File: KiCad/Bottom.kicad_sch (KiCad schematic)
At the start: 31 parts, among them J162 Screw_Terminal_01x02

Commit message: WIP on Bottom
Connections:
- net +3.3V: now also U?.16 (GPIO12)
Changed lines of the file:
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@@
+    (effects (font (size 1.27 1.27)) (justify right))
+  )
+  (hierarchical_label "+3.3V" (shape input) (at 96.52 113.03 180) (fields_autoplaced)
     (effects (font (size 1.27 1.27)) (justify right))
   )

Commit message: Layout wip
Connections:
- net SPI1_CSn renamed SPI_CSn_BOT
- net SPI1_RST renamed SPI0_RST
- net SPI1_RX renamed SPI_RX_BOT
- net SPI1_SCK renamed SPI_SCK_BOT
- net SPI1_TX renamed SPI_TX_BOT
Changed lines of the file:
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@@
     (effects (font (size 1.27 1.27)) (justify left bottom))
   )
-  (label "SPI1_RST" (at 85.09 100.33 0) (fields_autoplaced)
+  (label "SPI0_RST" (at 85.09 100.33 0) (fields_autoplaced)
     (effects (font (size 1.27 1.27)) (justify left bottom))
   )
@@
     (effects (font (size 1.27 1.27)) (justify left bottom))
   )
-  (label "SPI1_RST" (at 113.03 35.56 0) (fields_autoplaced)
+  (label "SPI0_RST" (at 113.03 35.56 0) (fields_autoplaced)
     (effects (font (size 1.27 1.27)) (justify left bottom))
   )
@@
     (effects (font (size 1.27 1.27)) (justify left bottom))
   )
-  (label "SPI0_RX" (at 35.56 129.54 0) (fields_autoplaced)
+  (label "SPI1_RX" (at 35.56 129.54 0) (fields_autoplaced)
     (effects (font (size 1.27 1.27)) (justify left bottom))
   )
@@
     (effects (font (size 1.27 1.27)) (justify left bottom))
   )
-  (label "SPI1_CSn" (at 113.03 27.94 0) (fields_autoplaced)
+  (label "SPI0_CSn" (at 113.03 27.94 0) (fields_autoplaced)
     (effects (font (size 1.27 1.27)) (justify left bottom))
   )
@@
     (effects (font (size 1.27 1.27)) (justify left bottom))
   )
-  (label "SPI0_CSn" (at 35.56 132.08 0) (fields_autoplaced)
+  (label "SPI1_CSn" (at 35.56 132.08 0) (fields_autoplaced)
     (effects (font (size 1.27 1.27)) (justify left bottom))
   )
@@
     (effects (font (size 1.27 1.27)) (justify left bottom))
   )
-  (label "SPI0_TX" (at 35.56 137.16 0) (fields_autoplaced)
+  (label "SPI1_TX" (at 35.56 137.16 0) (fields_autoplaced)
     (effects (font (size 1.27 1.27)) (justify left bottom))
   )
@@
     (effects (font (size 1.27 1.27)) (justify left bottom))
   )
-  (label "SPI1_TX" (at 113.03 33.02 0) (fields_autoplaced)
+  (label "SPI0_TX" (at 113.03 33.02 0) (fields_autoplaced)
     (effects (font (size 1.27 1.27)) (justify left bottom))
   )
-  (label "SPI0_SCK" (at 35.56 134.62 0) (fields_autoplaced)
+  (label "SPI1_SCK" (at 35.56 134.62 0) (fields_autoplaced)
     (effects (font (size 1.27 1.27)) (justify left bottom))
   )
@@
     (effects (font (size 1.27 1.27)) (justify left bottom))
   )
-  (label "SPI1_SCK" (at 113.03 30.48 0) (fields_autoplaced)
+  (label "SPI0_SCK" (at 113.03 30.48 0) (fields_autoplaced)
     (effects (font (size 1.27 1.27)) (justify left bottom))
   )
@@
     (effects (font (size 1.27 1.27)) (justify left bottom))
   )
-  (hierarchical_label "SPI0_TX" (shape input) (at 29.21 137.16 180) (fields_autoplaced)
+  (hierarchical_label "SPI_TX_BOT" (shape input) (at 29.21 137.16 180) (fields_autoplaced)
     (effects (font (size 1.27 1.27)) (justify right))
   )
@@
     (effects (font (size 1.27 1.27)) (justify right))
   )
-  (hierarchical_label "SPI0_CSn" (shape input) (at 29.21 132.08 180) (fields_autoplaced)
+  (hierarchical_label "SPI_CSn_BOT" (shape input) (at 29.21 132.08 180) (fields_autoplaced)
     (effects (font (size 1.27 1.27)) (justify right))
   )
-  (hierarchical_label "SPI0_SCK" (shape input) (at 29.21 134.62 180) (fields_autoplaced)
+  (hierarchical_label "SPI_SCK_BOT" (shape input) (at 29.21 134.62 180) (fields_autoplaced)
     (effects (font (size 1.27 1.27)) (justify right))
   )
@@
     (effects (font (size 1.27 1.27)) (justify right))
   )
-  (hierarchical_label "SPI0_RX" (shape input) (at 29.21 129.54 180) (fields_autoplaced)
+  (hierarchical_label "SPI_RX_BOT" (shape input) (at 29.21 129.54 180) (fields_autoplaced)
     (effects (font (size 1.27 1.27)) (justify right))
   )

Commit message: Ready for review
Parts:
- U?: footprint Module_RaspberryPi_Pico:RaspberryPi_Pico_Original_SMD_Castellated_HandSolder -> Module_RaspberryPi_Pico:RaspberryPi_Pico_Common_No_Keepout
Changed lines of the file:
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@@
       (effects (font (size 1.27 1.27)) (justify left))
     )
-    (property "Footprint" "Module_RaspberryPi_Pico:RaspberryPi_Pico_Original_SMD_Castellated_HandSolder" (at 119.38 154.94 0)
+    (property "Footprint" "Module_RaspberryPi_Pico:RaspberryPi_Pico_Common_No_Keepout" (at 119.38 154.94 0)
       (effects (font (size 1.27 1.27)) hide)
     )

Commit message: Updated to generate JLCPCB files
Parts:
- added C127: RVT0J102M0810, footprint:CAP-SMD_BD8.0-L8.3-W8.3-FD, symbol RVT0J102M0810:RVT0J102M0810
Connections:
- net GND: now also C127.2
- net VDD: now also C127.1
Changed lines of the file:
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@@
+    (effects (font (size 1.27 1.27)) (justify right))
+  )
+  (hierarchical_label "GND" (shape input) (at 242.57 48.26 270) (fields_autoplaced)
     (effects (font (size 1.27 1.27)) (justify right))
   )
@@
   (hierarchical_label "GND" (shape input) (at 231.14 67.31 180) (fields_autoplaced)
     (effects (font (size 1.27 1.27)) (justify right))
+  )
+  (hierarchical_label "VDD" (shape input) (at 242.57 40.64 90) (fields_autoplaced)
+    (effects (font (size 1.27 1.27)) (justify left))
   )
   (hierarchical_label "VDD" (shape input) (at 119.38 48.26 90) (fields_autoplaced)
@@
         )
       )
+    )
+  )
+  (symbol (lib_id "RVT0J102M0810:RVT0J102M0810") (at 242.57 44.45 0) (unit 1)
+    (in_bom yes) (on_board yes) (dnp no) (fields_autoplaced)
+    (property "Reference" "C127" (at 246.38 41.9139 0)
+      (effects (font (size 1.27 1.27)) (justify left))
+    )
+    (property "Value" "RVT0J102M0810" (at 246.38 44.4539 0)
+      (effects (font (size 1.27 1.27)) (justify left))
+    )
+    (property "Footprint" "footprint:CAP-SMD_BD8.0-L8.3-W8.3-FD" (at 242.57 54.61 0)
+      (effects (font (size 1.27 1.27) italic) hide)
+    )
+    (property "Datasheet" "https://item.szlcsc.com/245644.html" (at 240.284 44.323 0)
+      (effects (font (size 1.27 1.27)) (justify left) hide)
+    )
+    (property "LCSC" "C42851" (at 242.57 44.45 0)
+      (effects (font (size 1.27 1.27)) hide)
+    )
+    (pin "1")
+    (pin "2")
+    (instances
+      (project "Kaboom_box"
+        (path "/8d340784-229e-46d1-990c-7f8852f9fc49/d111de2c-3c3c-486e-8c4b-bd3963817676"
+          (reference "C127") (unit 1)
+        )
+      )

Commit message: PCB V1
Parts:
- R? (x2): now not fitted
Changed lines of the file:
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@@
   )
   (symbol (lib_id "0805W8F0000T5E:0805W8F0000T5E") (at 267.97 66.04 0) (unit 1)
-    (in_bom yes) (on_board yes) (dnp no) (fields_autoplaced)
+    (in_bom yes) (on_board yes) (dnp yes) (fields_autoplaced)
     (property "Reference" "R?" (at 267.97 59.69 0)
       (effects (font (size 1.27 1.27)))
@@
   )
   (symbol (lib_id "0805W8F0000T5E:0805W8F0000T5E") (at 267.97 76.2 0) (unit 1)
-    (in_bom yes) (on_board yes) (dnp no) (fields_autoplaced)
+    (in_bom yes) (on_board yes) (dnp yes) (fields_autoplaced)
     (property "Reference" "R?" (at 267.97 69.85 0)
       (effects (font (size 1.27 1.27)))

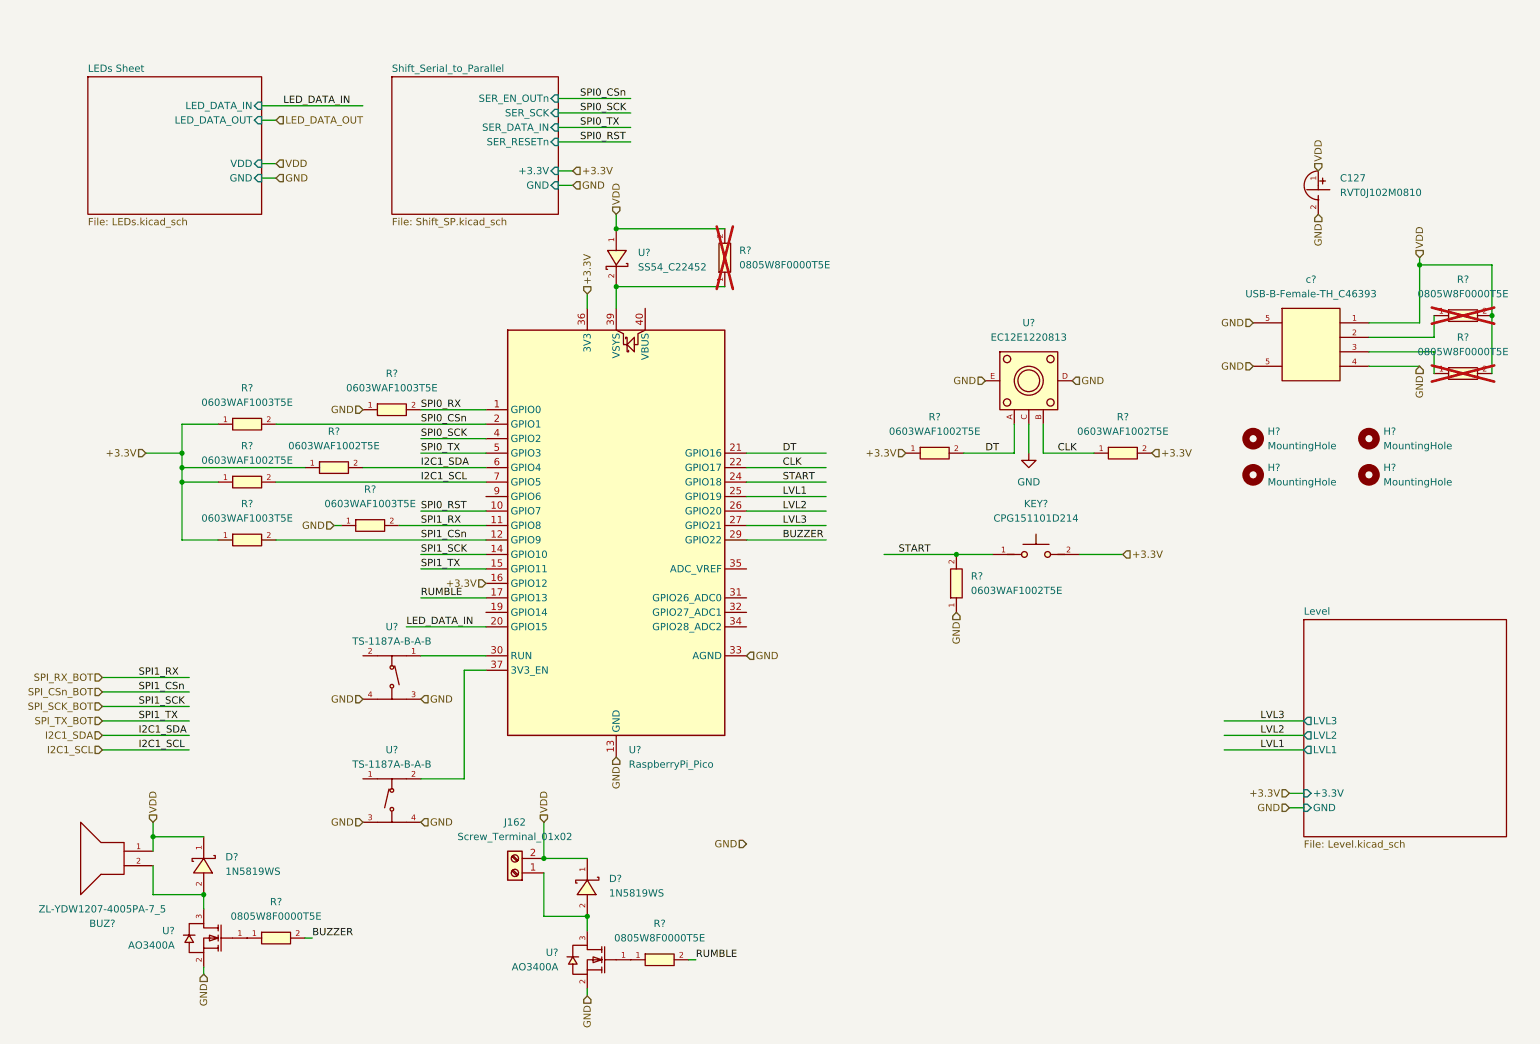
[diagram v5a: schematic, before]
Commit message: UPdated outline + added pull down resistors on input of shifts
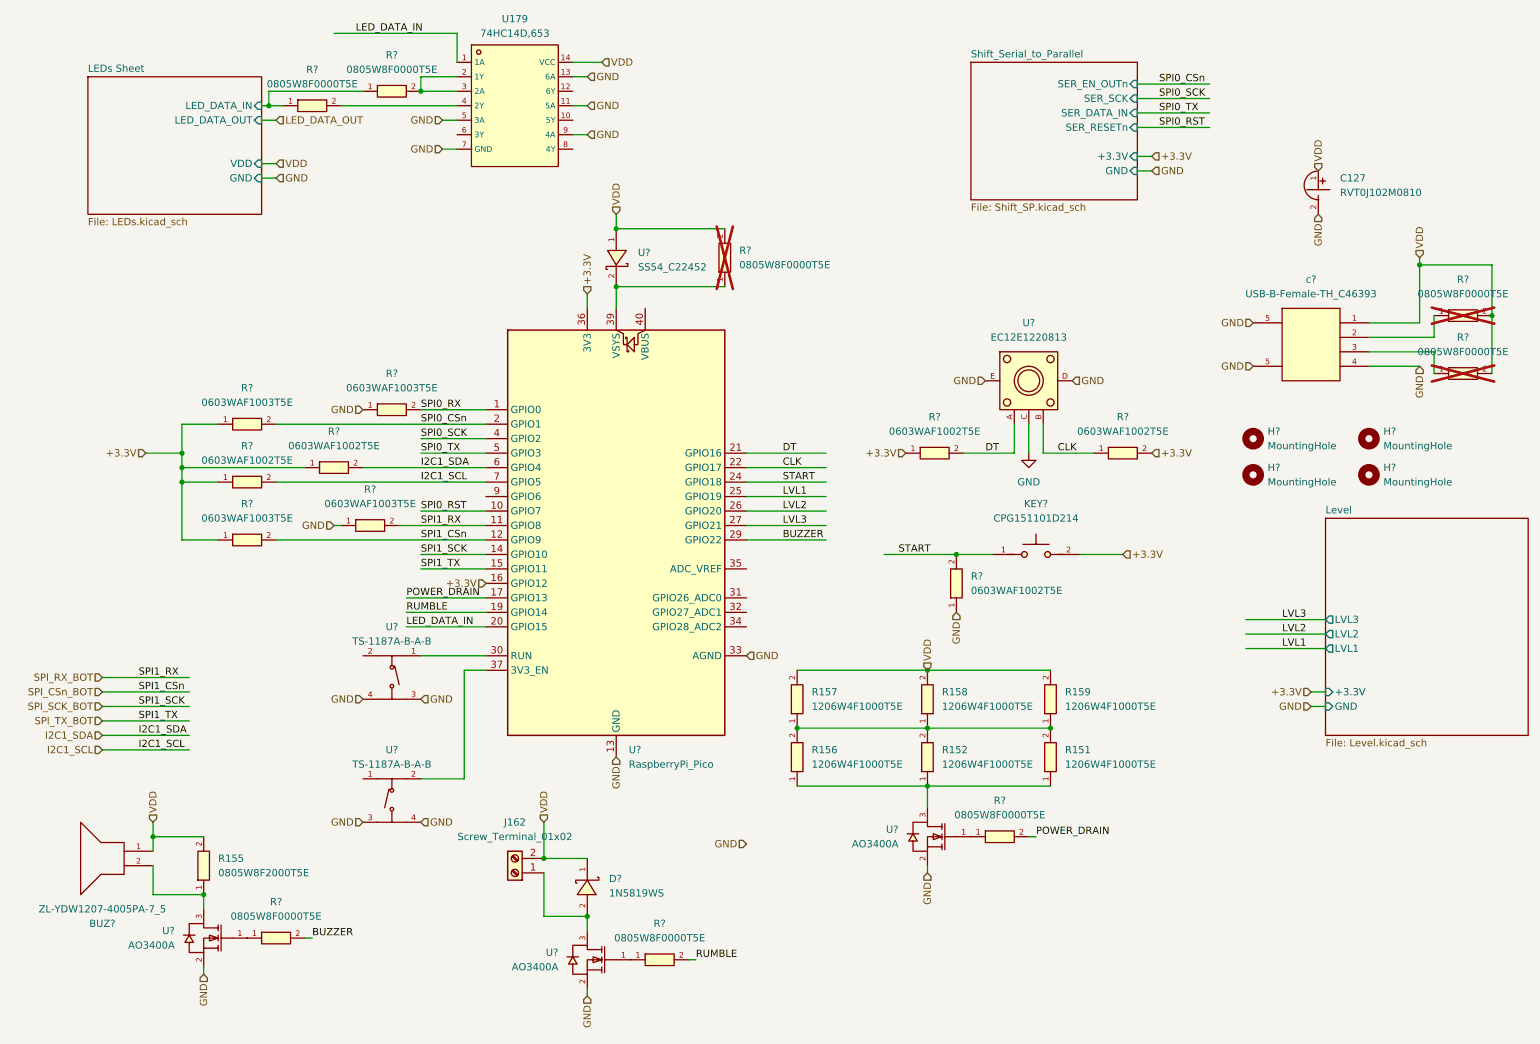
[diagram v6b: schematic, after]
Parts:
- removed D?: 1N5819WS, footprint:SOD-323_L1.8-W1.3-LS2.5-RD, symbol 1N5819WS:1N5819WS
- added R151, R152, R156, R157, R158, R159: 1206W4F1000T5E, footprint:R1206, symbol 1206W4F1000T5E:1206W4F1000T5E
- added R155: 0805W8F2000T5E, footprint:R0805, symbol 0805W8F2000T5E:0805W8F2000T5E
- added R? (x3): 0805W8F0000T5E, footprint:R0805, symbol 0805W8F0000T5E:0805W8F0000T5E
- added U179: 74HC14D,653, footprint:SOIC-14_L8.7-W3.9-P1.27-LS6.0-BL, symbol 74HC14D,653:74HC14D,653
- added U?: AO3400A, footprint:SOT-23-3_L2.9-W1.6-P1.90-LS2.8-BR, symbol AO3400A:AO3400A
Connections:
- net GND: now also U179.11 (5A), U179.13 (6A), U179.5 (3A), U179.7 (GND), U179.9 (4A), U?.2 (S)
- net LED_DATA_IN: now also U179.1 (1A)
- net RUMBLE: now also U?.19 (GPIO14); no longer U?.17 (GPIO13)
- net VDD: now also R155.2, R157.2, R158.2, R159.2, U179.14 (VCC)
- net at BUZ?.2, U?.3 (D): now also R155.1
- new net: R?.2, U179.2 (1Y), U179.3 (2A)
- new net: R?.2, U179.4 (2Y)
- new net: R151.2, R152.2, R156.2, R157.1, R158.1, R159.1
- new net: R151.1, R152.1, R156.1, U?.3 (D)
- new net: R?.1, U?.1 (G)
- new net LEDs Sheet/LED_DATA_IN: R?.1, R?.1
- new net POWER_DRAIN: R?.2, U?.17 (GPIO13)

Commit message: Updates for V2
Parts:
- added C?: CC0603KRX7R9BB104, footprint:C0603, symbol CC0603KRX7R9BB104:CC0603KRX7R9BB104
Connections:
- net GND: now also C?.2
- net VDD: now also C?.1
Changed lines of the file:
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@@
+    (effects (font (size 1.27 1.27)) (justify right))
+  )
+  (hierarchical_label "VDD" (shape input) (at 96.52 48.26 180) (fields_autoplaced)
     (effects (font (size 1.27 1.27)) (justify right))
   )
@@
   )
   (hierarchical_label "VDD" (shape input) (at 242.57 40.64 90) (fields_autoplaced)
+    (effects (font (size 1.27 1.27)) (justify left))
+  )
+  (hierarchical_label "GND" (shape input) (at 106.68 48.26 0) (fields_autoplaced)
     (effects (font (size 1.27 1.27)) (justify left))
   )
@@
         )
       )
+    )
+  )
+  (symbol (lib_id "CC0603KRX7R9BB104:CC0603KRX7R9BB104") (at 101.6 48.26 0) (unit 1)
+    (in_bom yes) (on_board yes) (dnp no) (fields_autoplaced)
+    (property "Reference" "C?" (at 101.6 41.91 0)
+      (effects (font (size 1.27 1.27)))
+    )
+    (property "Value" "CC0603KRX7R9BB104" (at 101.6 44.45 0)
+      (effects (font (size 1.27 1.27)))
+    )
+    (property "Footprint" "footprint:C0603" (at 101.6 58.42 0)
+      (effects (font (size 1.27 1.27) italic) hide)
+    )
+    (property "Datasheet" "https://item.szlcsc.com/362304.html" (at 99.314 48.133 0)
+      (effects (font (size 1.27 1.27)) (justify left) hide)
+    )
+    (property "LCSC" "C14663" (at 101.6 48.26 0)
+      (effects (font (size 1.27 1.27)) hide)
+    )
+    (pin "1")
+    (pin "2")
+    (instances
+      (project "Kaboom_box"
+        (path "/8d340784-229e-46d1-990c-7f8852f9fc49"
+          (reference "C?") (unit 1)
+        )
+        (path "/8d340784-229e-46d1-990c-7f8852f9fc49/d111de2c-3c3c-486e-8c4b-bd3963817676"
+          (reference "C129") (unit 1)
+        )
+        (path "/8d340784-229e-46d1-990c-7f8852f9fc49/c9ccc42e-41d9-40f0-918f-9c4b4cc23369/b91a06cc-d8a4-43a7-b652-a0f7f13c3d33"
+          (reference "C?") (unit 1)
+        )
+        (path "/8d340784-229e-46d1-990c-7f8852f9fc49/d111de2c-3c3c-486e-8c4b-bd3963817676/919d5153-67ff-4420-984f-74490b836c87"
+          (reference "C109") (unit 1)
+        )
+      )

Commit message: First production
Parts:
- removed BUZ?: ZL-YDW1207-4005PA-7_5, footprint:BUZ-TH_BD12.6-P7.50-D0.9, symbol ZL-YDW1207-4005PA-7_5:ZL-YDW1207-4005PA-7_5
- removed D?: 1N5819WS, footprint:SOD-323_L1.8-W1.3-LS2.5-RD, symbol 1N5819WS:1N5819WS
- removed J162: Screw_Terminal_01x02, TerminalBlock_Phoenix:TerminalBlock_Phoenix_MKDS-1,5-2_1x02_P5.00mm_Horizontal, symbol Connector:Screw_Terminal_01x02
- removed R155: 0805W8F2000T5E, footprint:R0805, symbol 0805W8F2000T5E:0805W8F2000T5E
- removed R? (x2): 0805W8F0000T5E, footprint:R0805, symbol 0805W8F0000T5E:0805W8F0000T5E
- removed U? (x2): AO3400A, footprint:SOT-23-3_L2.9-W1.6-P1.90-LS2.8-BR, symbol AO3400A:AO3400A
- gave numbers to parts that had none: 28
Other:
- added sheet Physical (Physical.kicad_sch)
- added sheet RTC (RTC.kicad_sch)
